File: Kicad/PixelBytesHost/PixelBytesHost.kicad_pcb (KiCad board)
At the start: 4 copper layers, 48.5 x 84.2 mm, 79 parts, among them IC1 2536030320001, IC2 TC1108-2.8VDBTR, IC3 TPS61085TDGKR, J1 TC2030-MCP-NL, J2 Type - C, J3 B2B-XH-2__LF__SN_, Q1 SMMBT5551LT1G, Q2 SMMBT5551LT1G, Q3 SMMBT5551LT1G, U1 Pixel Bytes Display, U2 STM32F103CBTx, Y1 CX2520DB12000D0GPSC1

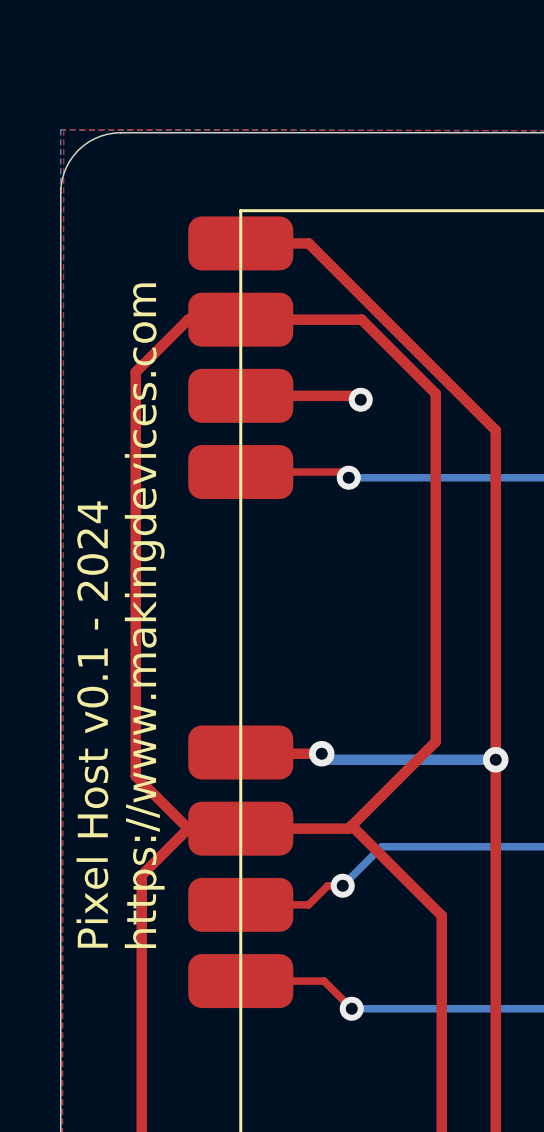
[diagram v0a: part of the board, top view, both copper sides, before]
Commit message: New firmware for the board
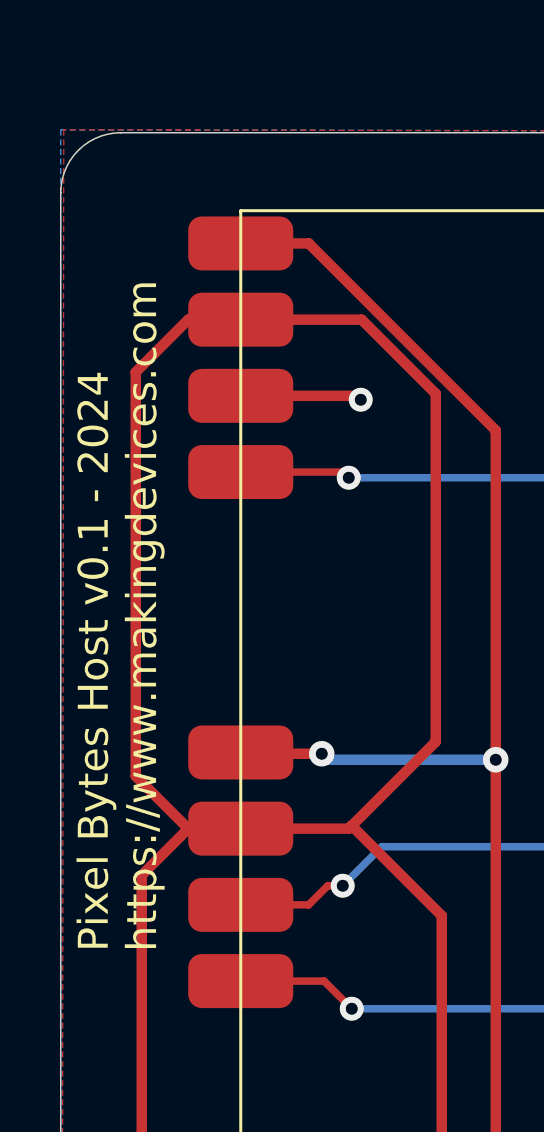
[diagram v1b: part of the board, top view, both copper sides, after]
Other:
- board text added: "Pixel Bytes Host v0.1 - 2024 https://www.makingdevices.com"
- board text removed: "Pixel Host v0.1 - 2024 https://www.makingdevices.com"
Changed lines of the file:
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@@
 			(drillshape 0)
 			(scaleselection 1)
-			(outputdirectory "gerbers/")
+			(outputdirectory "../../Gerber/Host/")
 		)
 	)
@@
 		(layer "B.SilkS")
 	)
+	(gr_poly
+		(pts
+			(xy 152.9 116.85) (xy 151.5 116.85) (xy 151.5 119.25) (xy 152.9 119.25)
+		)
+		(stroke
+			(width 0.1)
+			(type solid)
+		)
+		(fill solid)
+		(layer "B.Mask")
+	)
+	(gr_poly
+		(pts
+			(xy 155.9 116.85) (xy 157.3 116.85) (xy 157.3 119.25) (xy 155.9 119.25)
+		)
+		(stroke
+			(width 0.1)
+			(type solid)
+		)
+		(fill solid)
+		(layer "B.Mask")
+	)
+	(gr_poly
+		(pts
+			(xy 145.6 110.6) (xy 144.1 110.6) (xy 144.1 104.8) (xy 145.6 104.8)
+		)
+		(stroke
+			(width 0.1)
+			(type solid)
+		)
+		(fill solid)
+		(layer "F.Mask")
+	)
+	(gr_poly
+		(pts
+			(xy 143.6 102.8) (xy 143.6 104.3) (xy 137.8 104.3) (xy 137.8 102.8)
+		)
+		(stroke
+			(width 0.1)
+			(type solid)
+		)
+		(fill solid)
+		(layer "F.Mask")
+	)
+	(gr_poly
+		(pts
+			(xy 142 122.65) (xy 135 122.65) (xy 135 123.75) (xy 142 123.75)
+		)
+		(stroke
+			(width 0.1)
+			(type solid)
+		)
+		(fill solid)
+		(layer "F.Mask")
+	)
+	(gr_poly
+		(pts
+			(xy 129.1 101.2) (xy 128.5 101.2) (xy 128.5 102.6) (xy 129.1 102.6)
+		)
+		(stroke
+			(width 0.1)
+			(type solid)
+		)
+		(fill solid)
+		(layer "F.Mask")
+	)
+	(gr_poly
+		(pts
+			(xy 130.65 101.05) (xy 128.75 101.05) (xy 128.75 100.45) (xy 130.65 100.45)
+		)
+		(stroke
+			(width 0.1)
+			(type solid)
+		)
+		(fill solid)
+		(layer "F.Mask")
+	)
+	(gr_poly
+		(pts
+			(xy 135.8 104.8) (xy 137.3 104.8) (xy 137.3 110.6) (xy 135.8 110.6)
+		)
+		(stroke
+			(width 0.1)
+			(type solid)
+		)
+		(fill solid)
+		(layer "F.Mask")
+	)
+	(gr_poly
+		(pts
+			(xy 130.3 101.2) (xy 130.3 102.6) (xy 130.9 102.6) (xy 130.9 101.2)
+		)
+		(stroke
+			(width 0.1)
+			(type solid)
+		)
+		(fill solid)
+		(layer "F.Mask")
+	)
+	(gr_poly
+		(pts
+			(xy 130.65 102.75) (xy 128.75 102.75) (xy 128.75 103.4) (xy 130.65 103.4)
+		)
+		(stroke
+			(width 0.1)
+			(type solid)
+		)
+		(fill solid)
+		(layer "F.Mask")
+	)
+	(gr_poly
+		(pts
+			(xy 137.8 111.1) (xy 137.8 112.6) (xy 143.6 112.6) (xy 143.6 111.1)
+		)
+		(stroke
+			(width 0.1)
+			(type solid)
+		)
+		(fill solid)
+		(layer "F.Mask")
+	)
 	(gr_line
 		(start 113 128.5)
@@
 		)
 	)
-	(gr_text "Pixel Host v0.1 - 2024\nhttps://www.makingdevices.com"
+	(gr_text "Pixel Bytes Host v0.1 - 2024\nhttps://www.makingdevices.com"
 		(at 116.3 73.6 90)
 		(layer "F.SilkS")

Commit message: Subimos todos los archivos de la v0.25
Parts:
- removed the R8 at (148.4, 105.0)
- removed the R9 at (148.4, 107.0)
- removed REF**: OSHW-Logo2_7.3x6mm_SilkScreen, Symbol:OSHW-Logo2_7.3x6mm_SilkScreen
- added JP2: SolderJumper_2_Open, Jumper:SolderJumper-2_P1.3mm_Open_RoundedPad1.0x1.5mm, B.Cu at (155.8, 109.1)
- R8: renamed from R10; value 4k7 -> 1k5
- moved R16 0.07 mm to (136.5, 116.0)
- renumbered R12 to R10, R13 to R11, R14 to R12, R15 to R13, R16 to R14, R17 to R15, R18 to R16, R19 to R17, R20 to R18, R21 to R19, R22 to R20, R23 to R21, R24 to R22, R25 to R23, R26 to R24, R27 to R25, R28 to R26, R29 to R27, R30 to R28, R31 to R29, R11 to R9
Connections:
- C21 pad 2: display_main -> display_supply
- D1 pad 1: display_main -> display_supply
- IC3 pad 3: uc_enable_display -> In_Vcc
- IC_BMS_TP1 pad 5: C_BAT+ -> Vdc_battery
- Q3 pad 2: uc_enable_display -> display_main
- Q3 pad 3: In_Vcc -> display_supply
- R27 pad 1: display_main -> display_supply
- U1 pad 12: Net-(U1-Vdi_s6) -> unconnected-(U1-Vdo_s5-Pad12)
- U1 pad 17: Net-(U1-Vdi_s5) -> Net-(U1-Vdi_s6)
- U1 pad 21: unconnected-(U1-Vdo_s6-Pad21) -> Net-(U1-Vdi_s5)
- U2 pad 32: Net-(U2-PA11) -> USB_D-
- U2 pad 33: Net-(U2-PA12) -> USB_D+
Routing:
- net display_supply: track 0.00 -> 40.6 mm, vias 0 -> 4
- net Vdc_battery: track 71.7 -> 108.9 mm, vias 1 -> 2
- net Net-(U1-Vdi_s5): track 53.5 -> 39.4 mm, vias 4 -> 2
- net uc_enable_display: track 29.6 -> 21.4 mm
- net USB_D+: track 35.1 -> 40.2 mm
- net USB_D-: track 30.4 -> 34.8 mm
- net Net-(U1-Vdi_s6): track 38.7 -> 35.1 mm, vias 2 -> 4
- net Net-(U2-PA12): track 3.21 -> 0.00 mm
- net Net-(U2-PA11): track 2.65 -> 0.00 mm
- net display_main: track 210.7 -> 212.5 mm, vias 10 -> 9
- net In_Vcc: track 52.6 -> 54.2 mm
- removed copper zone on In1.Cu, net Vgnd_main
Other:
- board text added: "Pixel Bytes Host V0.25 - 2024 https://www.makingdevices.com"
- board text removed: "Pixel Bytes Host v0.1 - 2024 https://www.makingdevices.com"

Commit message: Host HW 1.0 finished
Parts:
- removed the J2 at (138.5, 127.2)
- added J3: 629722000214, usb-c:629722000214, F.Cu at (138.6, 127.8)
- IC2: value TC1108-2.8VDBTR -> TC1108-3.3VDBTR
- SW_Toggle1: value K3-1260D-L1 -> 450302014072; footprint SamacSys_Parts:K31260DL1 -> User_3:450302014072
- Y1: value CX2520DB12000D0GPSC1 -> 830055663; footprint User_lib:CX2520DB12000D0GPSC1 -> User_3:830055663
- moved SW_Toggle1 5.52 mm to (119.3, 124.2)
- moved Y1 1.58 mm to (130.0, 105.8)
- moved C7 1.30 mm to (128.8, 102.5)
- moved C10 0.83 mm to (129.4, 123.6)
- moved R11 0.83 mm to (127.4, 123.6)
- moved R14 0.83 mm to (125.4, 123.6)
- moved C8 0.38 mm to (128.8, 108.8)
- renumbered J3 to J2
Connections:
- R29 pad 1: Net-(J2-CC2) -> Vgnd_main
- R29 pad 2: Vgnd_main -> Net-(J3-CC2)
- SW_Toggle1 pad 1: Vdc_battery -> In_Vcc
- SW_Toggle1 pad 2: In_Vcc -> Vdc_battery
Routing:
- net Net-(J2-CC2): track 14.1 -> 0.00 mm, vias 3 -> 0
- net BMS_Vcc: track 81.2 -> 72.7 mm, vias 5 -> 3
- net Net-(J3-CC2): track 0.00 -> 7.59 mm, vias 0 -> 1
- net Vdc_battery: track 108.9 -> 112.6 mm
- net In_Vcc: track 54.2 -> 57.8 mm
- net OSC2: track 14.1 -> 11.9 mm, vias 3 -> 1
- net OSC1: track 9.28 -> 7.71 mm
- net Vgnd_main: track 486.0 -> 487.5 mm, vias 25 -> 29
- net USB_D-: track 34.8 -> 34.1 mm
- net S_down: track 25.3 -> 25.9 mm
- added copper zone on In1.Cu, net Vgnd_main
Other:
- outline, holes or cut-outs redrawn
- board text added: "Pixel Bytes Host V1 - 2024 https://www.makingdevices.com"
- board text removed: "Pixel Bytes Host V0.25 - 2024 https://www.makingdevices.com"

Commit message: New Version PixelBytesHost
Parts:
- added G***: LOGO, Wurth Icon:Wurth, B.Cu at (128.9, 127.9)
- added LED_green_bms2: LTST-C171GKT, SamacSys_Parts:LEDC2012X90N, F.Cu at (144.2, 98.9)
- added R30: 3k3, SamacSys_Parts:RESC2012X65N, B.Cu at (159.7, 109.0)
- added R31: 10k, Resistor_SMD:R_0805_2012Metric, B.Cu at (143.7, 102.7)
- added R32: 1k, Resistor_SMD:R_0805_2012Metric, B.Cu at (144.3, 99.4)
- added S1: 434121025816, User_3:434121050816, B.Cu at (139.5, 104.0)
- C15, C7, C8: footprint SamacSys_Parts:CAPC2012X145N -> Capacitor_SMD:C_0805_2012Metric
- C18, C19, C20, C21: footprint User_lib:CAPC2012X140N -> SamacSys_Parts:CAPC2012X140N
- IC3: footprint User_lib:SOP65P490X110-8N -> SamacSys_Parts:SOP65P490X110-8N
- J1: footprint User_lib:TC2030-MCP-NL -> SamacSys_Parts:TC2030-MCP-NL
- L1: footprint User_lib:SRN6045_1 -> SamacSys_Parts:SRN6045_1
- Q3: value SMMBT5551LT1G -> PBSS5160T-QR; footprint SamacSys_Parts:SOT96P237X111-3N -> SamacSys_Parts:SOT95P230X110-3N
- R10, R13, R14, R16, R19, R20, R23, R24: footprint SamacSys_Parts:RESC2012X65N -> Resistor_SMD:R_0805_2012Metric
- R11, R12, R15, R17, R18, R9: footprint User_lib:RESC2012X75N -> Resistor_SMD:R_0805_2012Metric
- R2, R3: value 20K -> 10k
- R22: value 4k7 -> 6k8
- R26: footprint User_lib:RESC2012X75N -> SamacSys_Parts:RESC2012X75N
- R27: value 82k -> 100k; footprint User_lib:RESC2012X75N -> SamacSys_Parts:RESC2012X75N
- R28: value 27k -> 38.3k; footprint User_lib:RESC2012X75N -> SamacSys_Parts:RESC2012X75N
- R5, R6, R7: value 10K -> 10k
- S_a1, S_b1, S_down1, S_left1, S_right1, S_up1: footprint User_lib:430182070816 -> SamacSys_Parts:430182070816
- moved Q3 0.39 mm to (156.1, 112.5)
- moved R22 0.21 mm to (159.3, 112.2)
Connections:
- Q3 pad 2: display_main -> display_supply
- Q3 pad 3: display_supply -> display_main
- U2 pad 20: uc_enable_display -> boot1
- U2 pad 30: unconnected-(U2-PA9-Pad30) -> boot_led
- U2 pad 45: unconnected-(U2-PB8-Pad45) -> uc_enable_display
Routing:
- net boot1: track 0.00 -> 18.3 mm, vias 0 -> 1
- net uc_enable_display: track 21.4 -> 36.0 mm
- net boot_led: track 0.00 -> 10.9 mm, vias 0 -> 2
- net display_supply: track 40.6 -> 49.3 mm
- net Vgnd_main: track 487.5 -> 492.2 mm, vias 29 -> 30
- net display_main: track 212.5 -> 209.5 mm, vias 9 -> 10
- net Net-(Q3-B): track 2.05 -> 4.78 mm
- net Net-(LED_green_bms2-A): track 0.00 -> 2.34 mm, vias 0 -> 1
- net uc_supply: track 146.9 -> 146.1 mm, vias 15 -> 16
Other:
- board text added: "Pixel Bytes Host V1.25 - 2025 https://www.makingdevices.com"
- board text removed: "Pixel Bytes Host V1 - 2024 https://www.makingdevices.com"
